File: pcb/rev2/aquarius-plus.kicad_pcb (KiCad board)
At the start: 2 copper layers, 167 x 115 mm, 168 parts, among them J1 Cassette in, J10 Audio out, J11 Hand controller 2, J12 ESP USB Host, J13 Power in, J14 FPGA spare, J15 Expansion port, J16 ESP32 spare, J2 Cassette out, J3 TF-03A, J4 Printer, J5 Hand controller 1, J6 VGA, J7 DBG, Q1 BC847C, Q2 BC847C, Q3 2N7002, SW1 SW_DPDT_x2, U1 XC6SLX9-2TQG144C, U10 IS61C5128AS-25QLI, U11 SN74CB3T3245PWR, U15 LDL1117S33R, U17 LD1117S12, U2 SN74CB3T3245PWR, U3 MAX3221ECPWR, U4 SN74CB3T3245PWR, U5 ESP32-S3-WROOM-1-N4R2, U6 SN74CB3T3245PWR, U7 Z84C0010AEG, U8 SN74AHCT1G125DBVR, U9 SN74AHCT1G125DBVR, X1 SX3M14.31818M20F30TNN

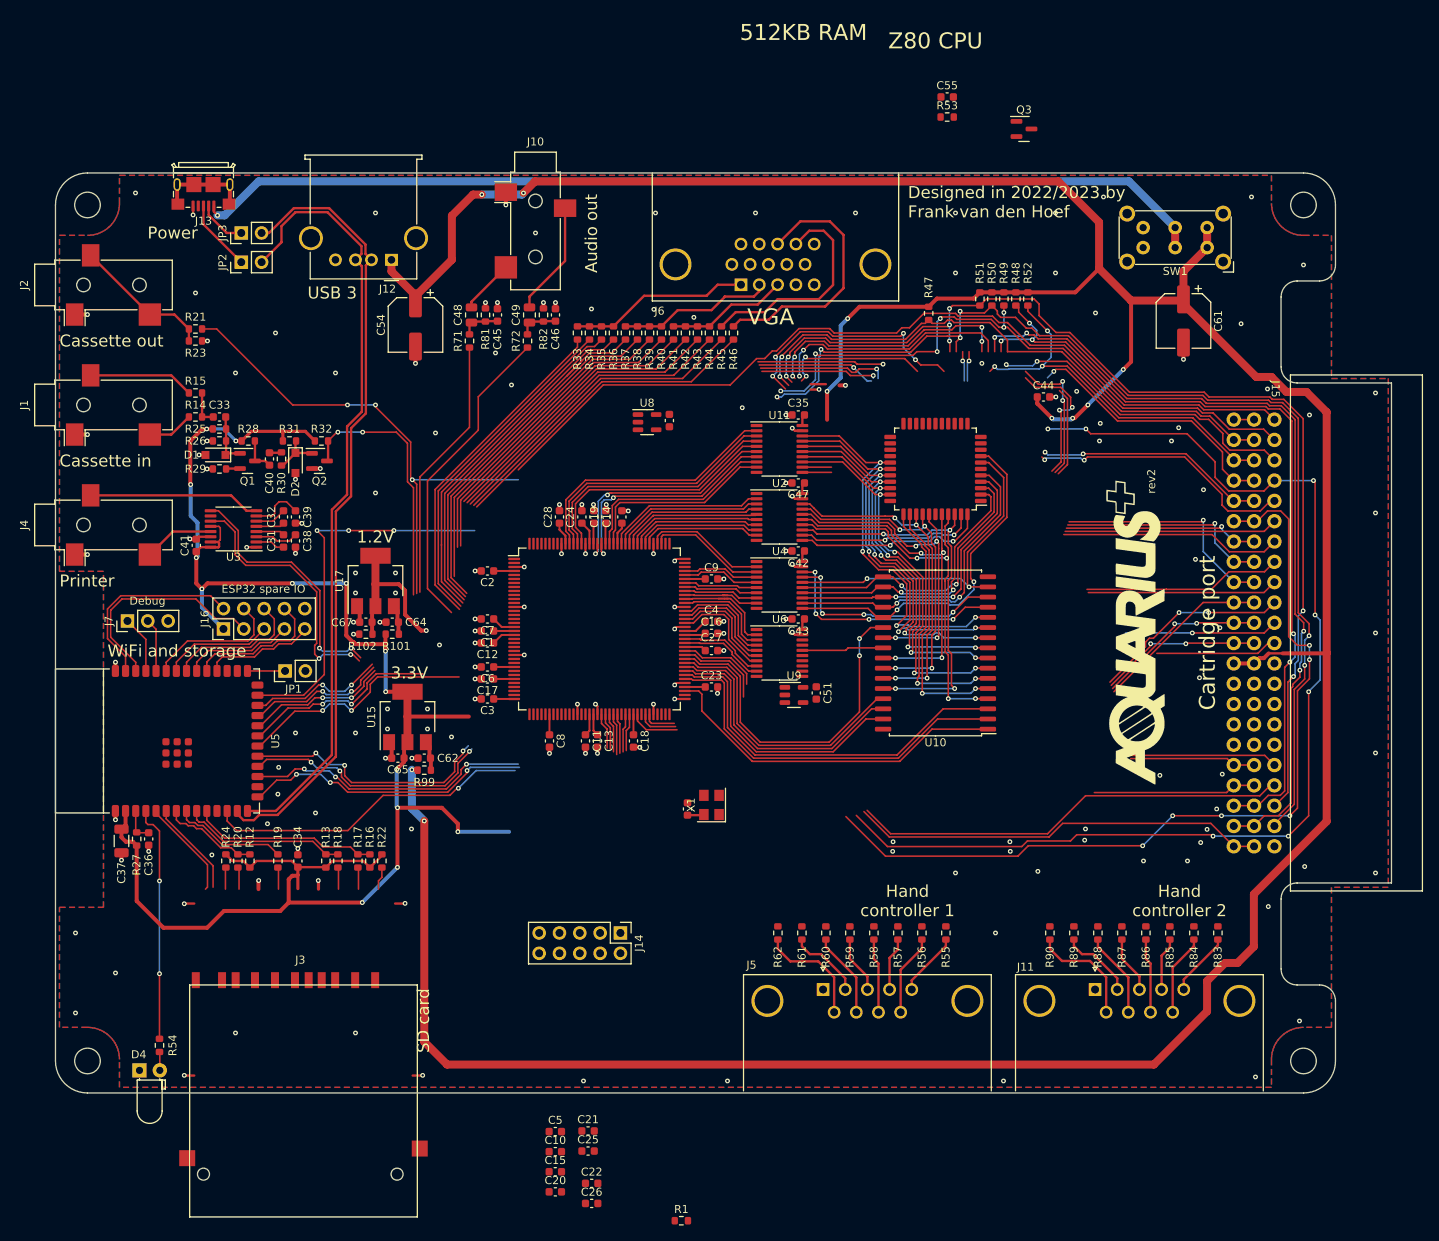
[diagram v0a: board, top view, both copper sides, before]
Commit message: Continued wiring rev2
Replaced the 2-lug USB micro power with a similar 4-lug model in the same family, orderable through JLCPCB.
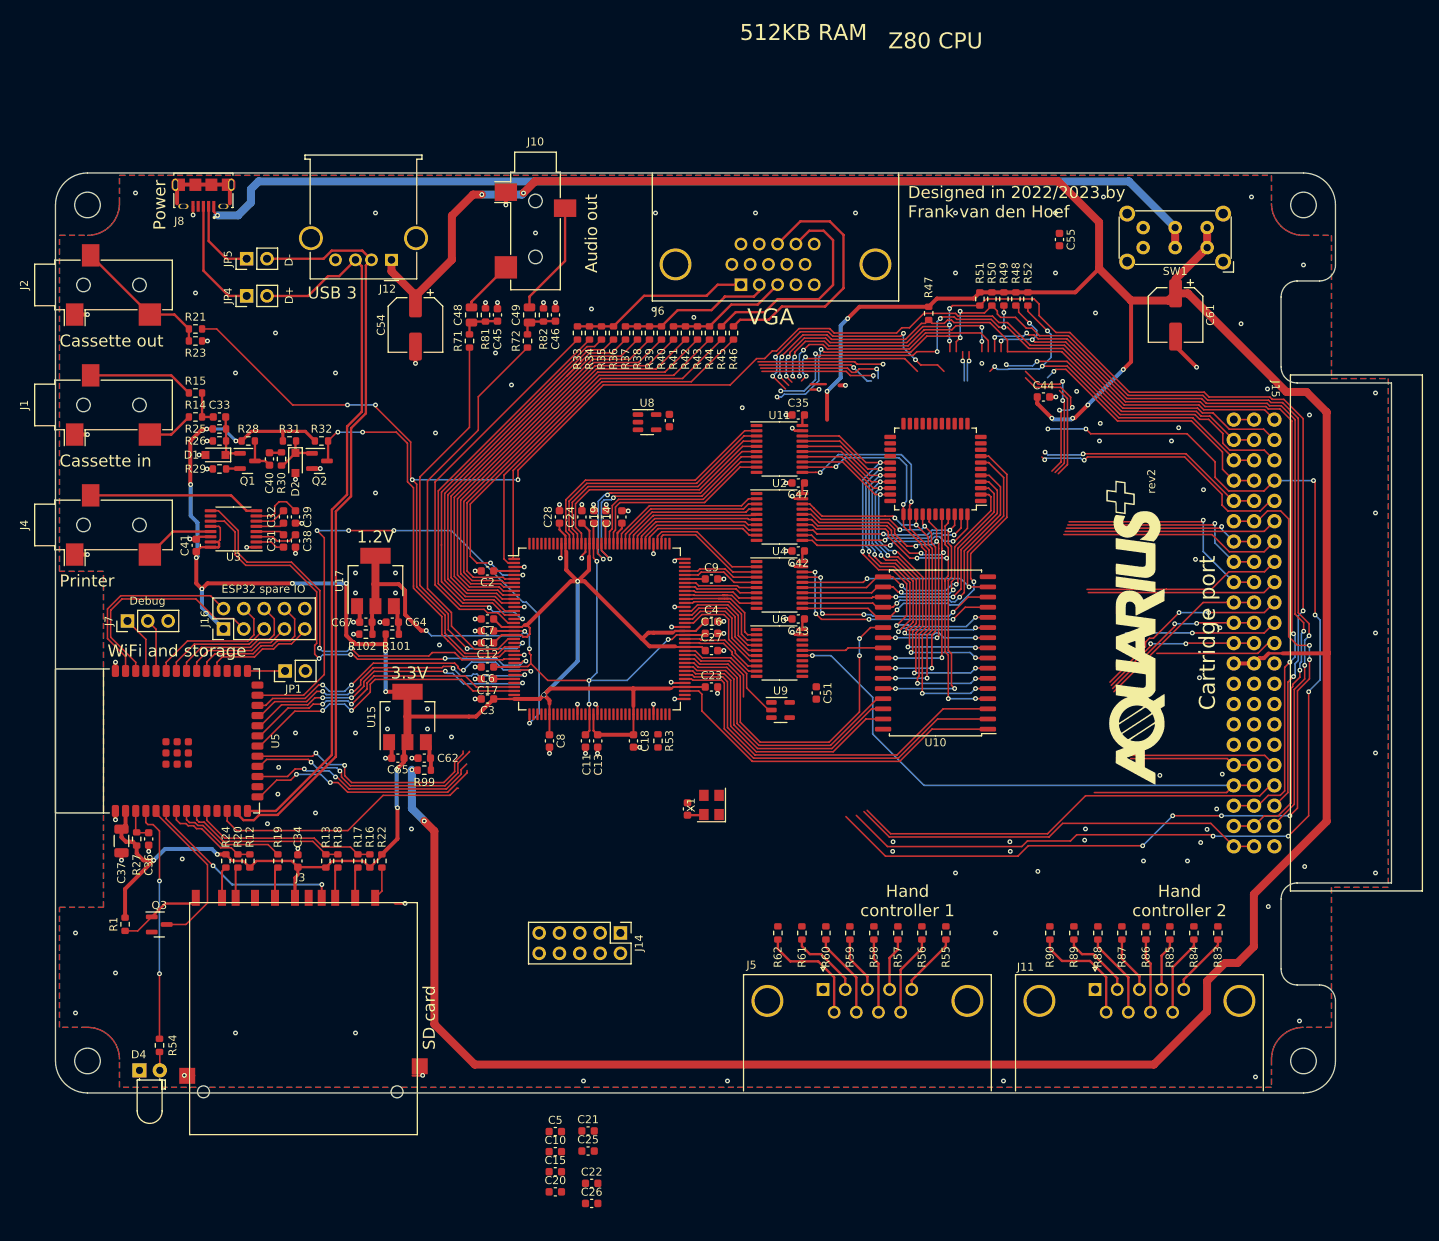
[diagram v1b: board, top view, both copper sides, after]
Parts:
- removed J13: Power in, aquarius-plus:10118193-0001LF
- removed JP2, JP3: USB, Connector_PinHeader_2.54mm:PinHeader_1x02_P2.54mm_Vertical
- added J8: Power in, aquarius-plus:AMPHENOL_10118194-0001LF, F.Cu at (83.5, 36.5)
- added JP4: USB, Connector_PinHeader_2.54mm:PinHeader_1x02_P2.54mm_Vertical, F.Cu at (88.9, 50.4)
- added JP5: USB, Connector_PinHeader_2.54mm:PinHeader_1x02_P2.54mm_Vertical, F.Cu at (88.9, 45.7)
- moved Q3 146.9 mm to (78.0, 128.9)
- moved R53 86.0 mm to (140.3, 106.0), turned to -90 degrees
- moved R1 78.8 mm to (73.7, 128.9), turned to 90 degrees
- moved C55 22.7 mm to (190.5, 43.3), turned to -90 degrees
- moved J3 10.3 mm to (96.0, 126.2)
- moved U9 2.52 mm to (155.6, 102.1)
- moved C61 1.24 mm to (205.0, 52.8)
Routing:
- net +1V2: track 33.0 -> 98.1 mm, vias 1 -> 7
- net WR#: track 24.1 -> 87.4 mm, vias 1 -> 2
- net +3V3: track 270.7 -> 328.3 mm, vias 15 -> 16
- net FPGA_PROG#: track 47.5 -> 75.0 mm, vias 3 -> 4
- net ESP_CTS: track 17.2 -> 40.6 mm, vias 2 -> 4
- net PRINTER_OUT: track 32.8 -> 55.7 mm, vias 2 -> 4
- net ESP_RX: track 17.3 -> 38.3 mm, vias 2 -> 4
- net ESP_RTS: track 17.5 -> 37.7 mm, vias 2 -> 4
- net PRINTER_IN: track 32.7 -> 52.4 mm
- net AUDIO_L: track 33.1 -> 50.9 mm, vias 0 -> 2
- net A7: track 63.6 -> 81.3 mm, vias 2 -> 4
- net CASSETTE_OUT: track 173.1 -> 190.8 mm, vias 3 -> 4
- net CASSETTE_IN: track 32.6 -> 49.5 mm
- net A6: track 62.1 -> 78.7 mm, vias 2 -> 4
- net VGA_B2: track 36.1 -> 51.8 mm
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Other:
- board text added: "D+"
- board text added: "D-"

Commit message: rev2 updates
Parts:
- added R2: 100, Resistor_SMD:R_0603_1608Metric, F.Cu at (152.4, 130.0)
- added R3: 100, Resistor_SMD:R_0603_1608Metric, F.Cu at (186.3, 130.0)
- moved C51 2.00 mm to (159.5, 101.9)
- turned R53 to 90 degrees
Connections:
- J11 pad 1: GND -> Net-(J11-Pad1)
- J5 pad 1: GND -> Net-(J5-Pad1)
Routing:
- net FPGA_PHI: track 11.1 -> 48.0 mm, vias 0 -> 2
- net FPGA_DONE: track 32.8 -> 68.1 mm, vias 0 -> 2
- net SPI_MOSI: track 29.2 -> 61.6 mm, vias 2 -> 6
- net SPI_CS#: track 30.7 -> 62.9 mm, vias 2 -> 6
- net SPI_SCLK: track 30.8 -> 58.6 mm, vias 2 -> 4
- net SYSCLK: track 0.00 -> 22.9 mm, vias 0 -> 2
- net +5V: track 457.6 -> 474.7 mm
- net SPI_MISO: track 29.3 -> 43.9 mm, vias 2 -> 4
- net +3V3: track 328.3 -> 341.5 mm, vias 16 -> 15
- net Net-(J5-Pad1): track 0.00 -> 13.1 mm
- net Net-(J11-Pad1): track 0.00 -> 11.5 mm
- net BUSACK#: track 136.1 -> 129.7 mm, vias 6 -> 5
- net BUSREQ#: track 79.2 -> 74.0 mm, vias 6 -> 5
- net Net-(U1-B2_IO_CCLK): track 0.00 -> 2.68 mm

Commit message: Cleaned up PCB.
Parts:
- removed J16: ESP32 spare, Connector_PinHeader_2.54mm:PinHeader_2x05_P2.54mm_Vertical
- added J13: ESP32 spare, Connector_PinHeader_2.54mm:PinHeader_2x07_P2.54mm_Vertical, F.Cu at (139.7, 142.5)
- J10: renamed from J14; footprint Connector_PinHeader_2.54mm:PinHeader_2x05_P2.54mm_Vertical -> Connector_PinHeader_2.54mm:PinHeader_2x06_P2.54mm_Vertical
- moved C20 84.9 mm to (125.0, 79.2), turned to 90 degrees
- moved C21 76.8 mm to (141.0, 79.2), turned to 90 degrees
- moved #G1 71.4 mm to (135.2, 122.4), turned to 0 degrees
- moved C55 69.7 mm to (180.1, 112.2), turned to 0 degrees
- moved C33 69.1 mm to (121.2, 88.5), turned to 180 degrees
- moved C44 68.8 mm to (149.2, 97.1)
- moved C34 65.6 mm to (121.2, 90.0), turned to 180 degrees
- moved C53 55.2 mm to (142.9, 107.2), turned to -90 degrees
- moved C50 52.7 mm to (129.4, 107.2), turned to -90 degrees
- moved C35 49.9 mm to (133.3, 107.3), turned to -90 degrees
- moved R38 47.6 mm to (92.8, 109.2), turned to 0 degrees
- moved X1 38.8 mm to (114.5, 93.0), turned to -90 degrees
- moved C32 38.4 mm to (114.5, 89.8), turned to 180 degrees
- moved U2 37.1 mm to (162.2, 65.6)
- moved C9 36.9 mm to (165.0, 65.4)
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- renumbered C48 to C1, C43 to C10, C40 to C11, C67 to C12, C64 to C13, C3 to C14, C17 to C15, C6 to C16, C12 to C17, C1 to C18, C7 to C19, C45 to C2, C26 to C20, C5 to C21, C2 to C22, C41 to C23, C44 to C24, C31 to C25, C38 to C26, C32 to C27, C39 to C28, C35 to C29, C49 to C3, C8 to C30, C28 to C31, C29 to C32, C10 to C33, C21 to C34, C25 to C35, C11 to C36, C24 to C37, C13 to C38, C30 to C39, C46 to C4, C19 to C40, C47 to C41, C14 to C42, C18 to C43, C20 to C44, C42 to C45, C4 to C46, C65 to C47, C62 to C48, C23 to C49, C61 to C5, C15 to C50, C27 to C51, C16 to C52, C22 to C53, C9 to C54, C34 to C56, C36 to C57, C37 to C58, C33 to C6, C54 to C7, C50 to C8, C51 to C9, D4 to D3, J8 to J1, J5 to J12, J12 to J2, J10 to J3, J6 to J4, J2 to J5, J1 to J6, J15 to J7, J4 to J8, J3 to J9, JP4 to JP1, JP5 to JP2, JP1 to JP3, J7 to JP4, R21 to R1, R45 to R10, R34 to R11, R38 to R12, R42 to R13, R46 to R14, R35 to R15, R39 to R16, R43 to R17, R15 to R18, R36 to R19, R23 to R2, R40 to R20, R44 to R21, R14 to R22, R52 to R23, R49 to R24, R51 to R25, R50 to R26, R48 to R27, R47 to R28, R28 to R29, R81 to R3, R32 to R30, R25 to R31, R26 to R32, R29 to R33, R30 to R34, R31 to R35, R102 to R36, R101 to R37, R53 to R38, R99 to R39, R71 to R4, R24 to R40, R20 to R41, R12 to R42, R19 to R43, R13 to R44, R18 to R45, R17 to R46, R16 to R47, R22 to R48, R27 to R49, R82 to R5, R2 to R50, R62 to R51, R61 to R52, R60 to R53, R59 to R54, R58 to R55, R57 to R56, R56 to R57, R55 to R58, R3 to R59, R72 to R6, R90 to R60, R89 to R61, R88 to R62, R87 to R63, R86 to R64, R85 to R65, R84 to R66, R83 to R67, R1 to R68, R54 to R69, R33 to R7, R37 to R8, R41 to R9, U8 to U1, U5 to U10, U15 to U11, U4 to U12, U10 to U13, U9 to U2, U17 to U3, U6 to U4, U3 to U5, U1 to U6, U11 to U8, U2 to U9
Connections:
- net ESP_USB_DM renamed ESP_USB_D-
- net ESP_USB_DP renamed ESP_USB_D+
- net Net-(J8-D+) renamed /USB_D+
- net Net-(J8-D-) renamed /USB_D-
- J10 pad 10: GND -> FPGA_EXP8
- J10 pad 9: unconnected-(J14-Pin_9-Pad9) -> FPGA_EXP7
- U10 pad 11: unconnected-(U5-IO18-Pad11) -> ESP_EXP10
- U10 pad 28: unconnected-(U5-IO35-Pad28) -> ESP_EXP9
- U10 pad 29: unconnected-(U5-IO36-Pad29) -> ESP_EXP8
- U6 pad 1: VGA_HSYNC -> FPGA_PHI
- U6 pad 10: VGA_G1 -> FPGA_RD#
- U6 pad 100: FPGA_D6 -> BA16
- U6 pad 101: FPGA_D5 -> BA14
- U6 pad 102: FPGA_D4 -> BA15
- U6 pad 104: FPGA_D3 -> BA18
- U6 pad 105: FPGA_D2 -> RAM_WE#
- U6 pad 11: VGA_G2 -> FPGA_IORQ#
- U6 pad 111: FPGA_D1 -> RAM_CE#
- U6 pad 112: FPGA_D0 -> FPGA_D7
- U6 pad 114: FPGA_A15 -> FPGA_D6
- U6 pad 115: FPGA_A14 -> FPGA_D5
- U6 pad 116: FPGA_A13 -> FPGA_D4
- U6 pad 117: FPGA_A12 -> FPGA_D3
- U6 pad 118: FPGA_A11 -> FPGA_D2
- U6 pad 119: FPGA_A10 -> FPGA_D1
- U6 pad 12: VGA_G3 -> FPGA_MREQ#
- U6 pad 120: FPGA_A9 -> FPGA_D0
- U6 pad 121: FPGA_A8 -> FPGA_A15
- U6 pad 123: FPGA_A7 -> FPGA_A14
- U6 pad 124: FPGA_A6 -> FPGA_A13
- U6 pad 126: FPGA_A5 -> FPGA_A12
- U6 pad 127: FPGA_A4 -> FPGA_A11
- U6 pad 131: FPGA_A3 -> FPGA_A10
- U6 pad 132: FPGA_A2 -> FPGA_A9
- U6 pad 133: FPGA_A1 -> FPGA_A8
- U6 pad 134: FPGA_A0 -> FPGA_A7
- U6 pad 137: unconnected-(U1-B0_IO-Pad137) -> FPGA_A6
- U6 pad 138: unconnected-(U1-B0_IO-Pad138) -> FPGA_A5
- U6 pad 139: unconnected-(U1-B0_IO-Pad139) -> FPGA_A4
- U6 pad 14: VGA_R0 -> VGA_HSYNC
- U6 pad 140: unconnected-(U1-B0_IO-Pad140) -> FPGA_A3
- U6 pad 141: unconnected-(U1-B0_IO-Pad141) -> FPGA_A2
- U6 pad 142: unconnected-(U1-B0_IO-Pad142) -> FPGA_A1
- U6 pad 143: unconnected-(U1-B0_IO_VREF-Pad143) -> FPGA_A0
- U6 pad 15: VGA_R1 -> VGA_VSYNC
- U6 pad 16: VGA_R2 -> VGA_B0
- U6 pad 17: VGA_R3 -> VGA_B1
- U6 pad 2: VGA_VSYNC -> FPGA_CART_CE#
- U6 pad 21: AUDIO_R -> VGA_B2
- U6 pad 22: AUDIO_L -> VGA_B3
- U6 pad 23: CASSETTE_OUT -> VGA_G0
- U6 pad 24: CASSETTE_IN -> VGA_G1
- U6 pad 26: PRINTER_IN -> VGA_G2
- U6 pad 27: PRINTER_OUT -> VGA_G3
- U6 pad 29: ESP_CTS -> VGA_R0
- U6 pad 30: ESP_RX -> VGA_R1
- U6 pad 32: ESP_RTS -> VGA_R2
- U6 pad 33: ESP_TX -> VGA_R3
- U6 pad 34: ESP_NOTIFY -> AUDIO_R
- U6 pad 35: unconnected-(U1-B3_IO-Pad35) -> AUDIO_L
- U6 pad 38: unconnected-(U1-B2_IO-Pad38) -> CASSETTE_OUT
- U6 pad 40: unconnected-(U1-B2_IO-Pad40) -> CASSETTE_IN
- U6 pad 41: unconnected-(U1-B2_IO-Pad41) -> PRINTER_IN
- U6 pad 43: unconnected-(U1-B2_IO-Pad43) -> PRINTER_OUT
- U6 pad 44: unconnected-(U1-B2_IO-Pad44) -> ESP_CTS
- U6 pad 45: unconnected-(U1-B2_IO-Pad45) -> ESP_RX
- U6 pad 46: unconnected-(U1-B2_IO-Pad46) -> ESP_RTS
- U6 pad 47: unconnected-(U1-B2_IO_VREF-Pad47) -> ESP_TX
- U6 pad 48: unconnected-(U1-B2_IO-Pad48) -> ESP_NOTIFY
- U6 pad 5: VGA_B0 -> FPGA_BUSACK#
- U6 pad 50: unconnected-(U1-B2_IO_GCLK30-Pad50) -> FPGA_EXP9
- U6 pad 51: unconnected-(U1-B2_IO_GCLK31-Pad51) -> FPGA_EXP8
- U6 pad 56: unconnected-(U1-B2_IO_GCLK1-Pad56) -> FPGA_EXP7
- U6 pad 57: unconnected-(U1-B2_IO-Pad57) -> FPGA_EXP6
- U6 pad 58: unconnected-(U1-B2_IO-Pad58) -> FPGA_EXP5
- U6 pad 59: unconnected-(U1-B2_IO-Pad59) -> FPGA_EXP4
- U6 pad 6: VGA_B1 -> FPGA_BUSREQ#
- U6 pad 61: unconnected-(U1-B2_IO-Pad61) -> FPGA_EXP3
- U6 pad 62: unconnected-(U1-B2_IO-Pad62) -> FPGA_EXP2
- U6 pad 64: unconnected-(U1-B2_IO-Pad64) -> FPGA_EXP1
- U6 pad 66: unconnected-(U1-B2_IO-Pad66) -> FPGA_EXP0
- U6 pad 67: unconnected-(U1-B2_IO-Pad67) -> HC1_D08
- U6 pad 7: VGA_B2 -> FPGA_RESET#
- U6 pad 75: BA17 -> HC1_D00
- U6 pad 78: BA16 -> HC1_D07
- U6 pad 79: BA14 -> HC1_D01
- U6 pad 8: VGA_B3 -> FPGA_INT#
- U6 pad 80: BA15 -> HC1_D06
- U6 pad 81: BA18 -> HC1_D02
- U6 pad 82: RAM_WE# -> HC1_D05
- U6 pad 83: RAM_CE# -> HC1_D03
- U6 pad 84: FPGA_PHI -> HC1_D04
- U6 pad 85: FPGA_CART_CE# -> HC2_D08
- U6 pad 87: FPGA_BUSACK# -> HC2_D00
- U6 pad 88: FPGA_BUSREQ# -> HC2_D07
- U6 pad 9: VGA_G0 -> FPGA_WR#
- U6 pad 92: FPGA_RESET# -> HC2_D01
- U6 pad 93: FPGA_INT# -> HC2_D06
- U6 pad 94: FPGA_WR# -> HC2_D02
- U6 pad 95: FPGA_RD# -> HC2_D05
- U6 pad 97: FPGA_IORQ# -> HC2_D03
- U6 pad 98: FPGA_MREQ# -> HC2_D04
- U6 pad 99: FPGA_D7 -> BA17
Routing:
- net +3V3: track 341.5 -> 529.2 mm, vias 15 -> 30
- net HC2_D08: track 0.00 -> 82.4 mm, vias 0 -> 2
- net HC2_D04: track 0.00 -> 80.8 mm
- net ESP_EXP0: track 24.5 -> 104.9 mm, vias 0 -> 2
- net HC2_D07: track 0.00 -> 80.1 mm, vias 0 -> 2
- net HC2_D03: track 0.00 -> 79.9 mm
- net HC2_D00: track 0.00 -> 79.4 mm, vias 0 -> 2
- net HC2_D05: track 0.00 -> 79.3 mm
- net HC2_D02: track 0.00 -> 78.4 mm
- net ESP_EXP2: track 17.3 -> 95.3 mm, vias 0 -> 2
- net HC2_D06: track 0.00 -> 77.6 mm
- net ESP_EXP8: track 0.00 -> 77.4 mm, vias 0 -> 2
- net ESP_EXP7: track 0.00 -> 77.0 mm, vias 0 -> 2
- net HC2_D01: track 0.00 -> 76.8 mm
- net ESP_EXP3: track 13.8 -> 89.3 mm, vias 0 -> 2
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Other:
- board text added: "USB KBD"
- board text added: "rev2b"
- board text removed: "ESP32 spare IO"
- board text removed: "USB 3"
- board text removed: "rev2"
